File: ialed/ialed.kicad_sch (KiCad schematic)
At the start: 9 parts, among them Q1 2N7002

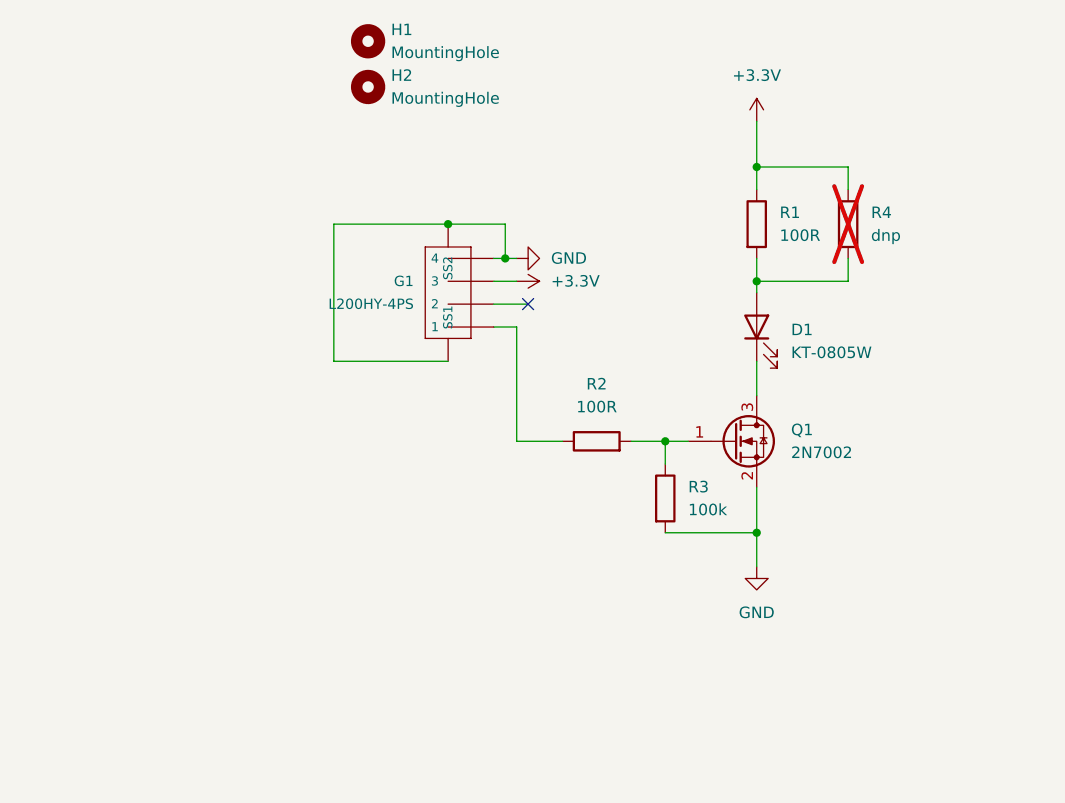
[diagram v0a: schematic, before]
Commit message: ialed v0.2: new version 0.2 including production data
I added a second small read LED to the free seed connector pin.
The production started on 16.9.2025 with a panel process a jlcpcb.
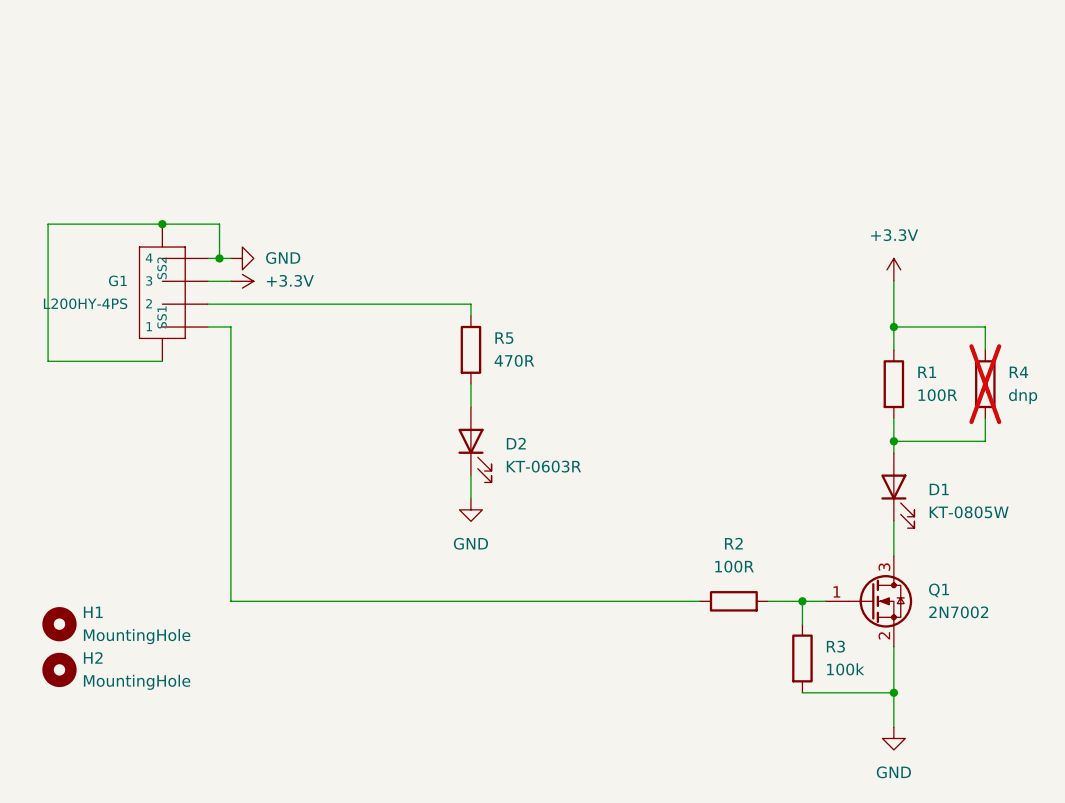
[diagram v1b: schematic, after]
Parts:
- added D2: KT-0603R, Diode_SMD:D_0603_1608Metric, symbol Device:LED
- added R5: 470R, Resistor_SMD:R_0603_1608Metric, symbol Device:R
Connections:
- net GND: now also D2.1 (K)
- net at G1.2: now also R5.1
- new net: D2.2 (A), R5.2
- no-connect marks 1 -> 0
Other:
- moved on the sheet: D1, G1, H1, H2, Q1, R1, R2, R3, R4
